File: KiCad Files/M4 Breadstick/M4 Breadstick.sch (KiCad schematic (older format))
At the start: 79 parts, among them IC1 ATSAMD51G_TQFN48, J10 D6|A6|RX, J11 D3|A3, J12 D4|A4, J13 D1|A1, J14 D14|SDA, J15 D20|A20, J16 D15|SCL, J17 D16, J18 D13|SCK, J19 D17, J2 3220-10-0300-00-TR, J20 D12|MISO, J21 VBUS, J22 D11|MOSI, J23 D10|COM3, J24 D9|COM2, J25 D8|SDA, J26 D7|SCL, J27 VBAT, J28 GND, J29 3.3V, J3 GND, J30 3.3V, J4 ~RESET, J5 D2|A2|LDAC, J6 AREF, J7 D19|A19, J8 D18|A18|RDAC, J9 D5|A5|TX, SW1 SMD-BUTTON_2P-3.0X2.5X1.2+0.4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, U1 SN74LVC2T45DCUR, U2 GD25x16, U3 NCP1117ST33T3G

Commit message: Multi sheets created
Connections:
- net VHI: no longer C1.1, C10.1, C9.1, D1.2 (-), D2.2 (-), U3.3 (IN)
- new net 5V: C1.1, C10.1, C9.1, D1.2 (-), D2.2 (-), U3.3 (IN)
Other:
- moved on the sheet: C1, C10, C2, C3, C4, C5, C6, C7, C8, C9, D1, D2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

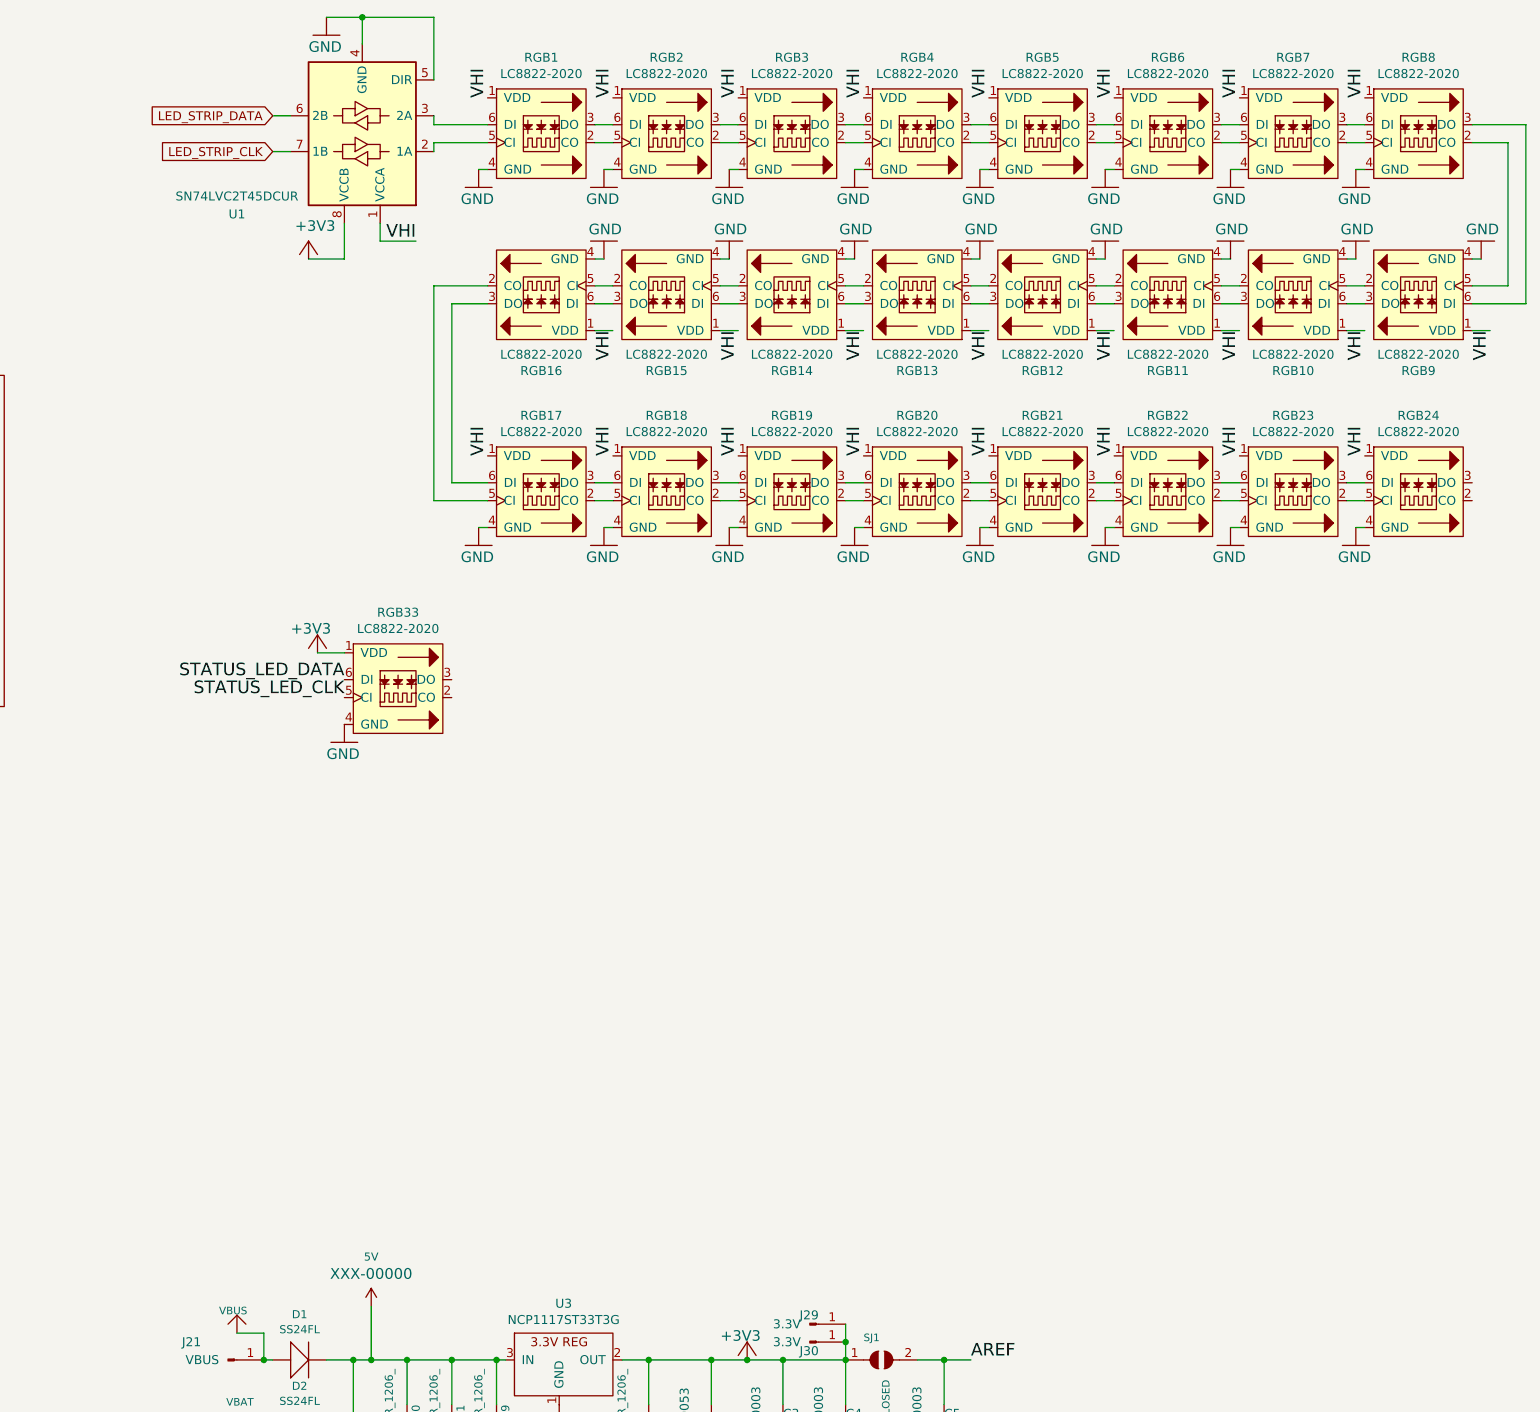
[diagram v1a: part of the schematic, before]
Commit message: LEDs moved to child sheet
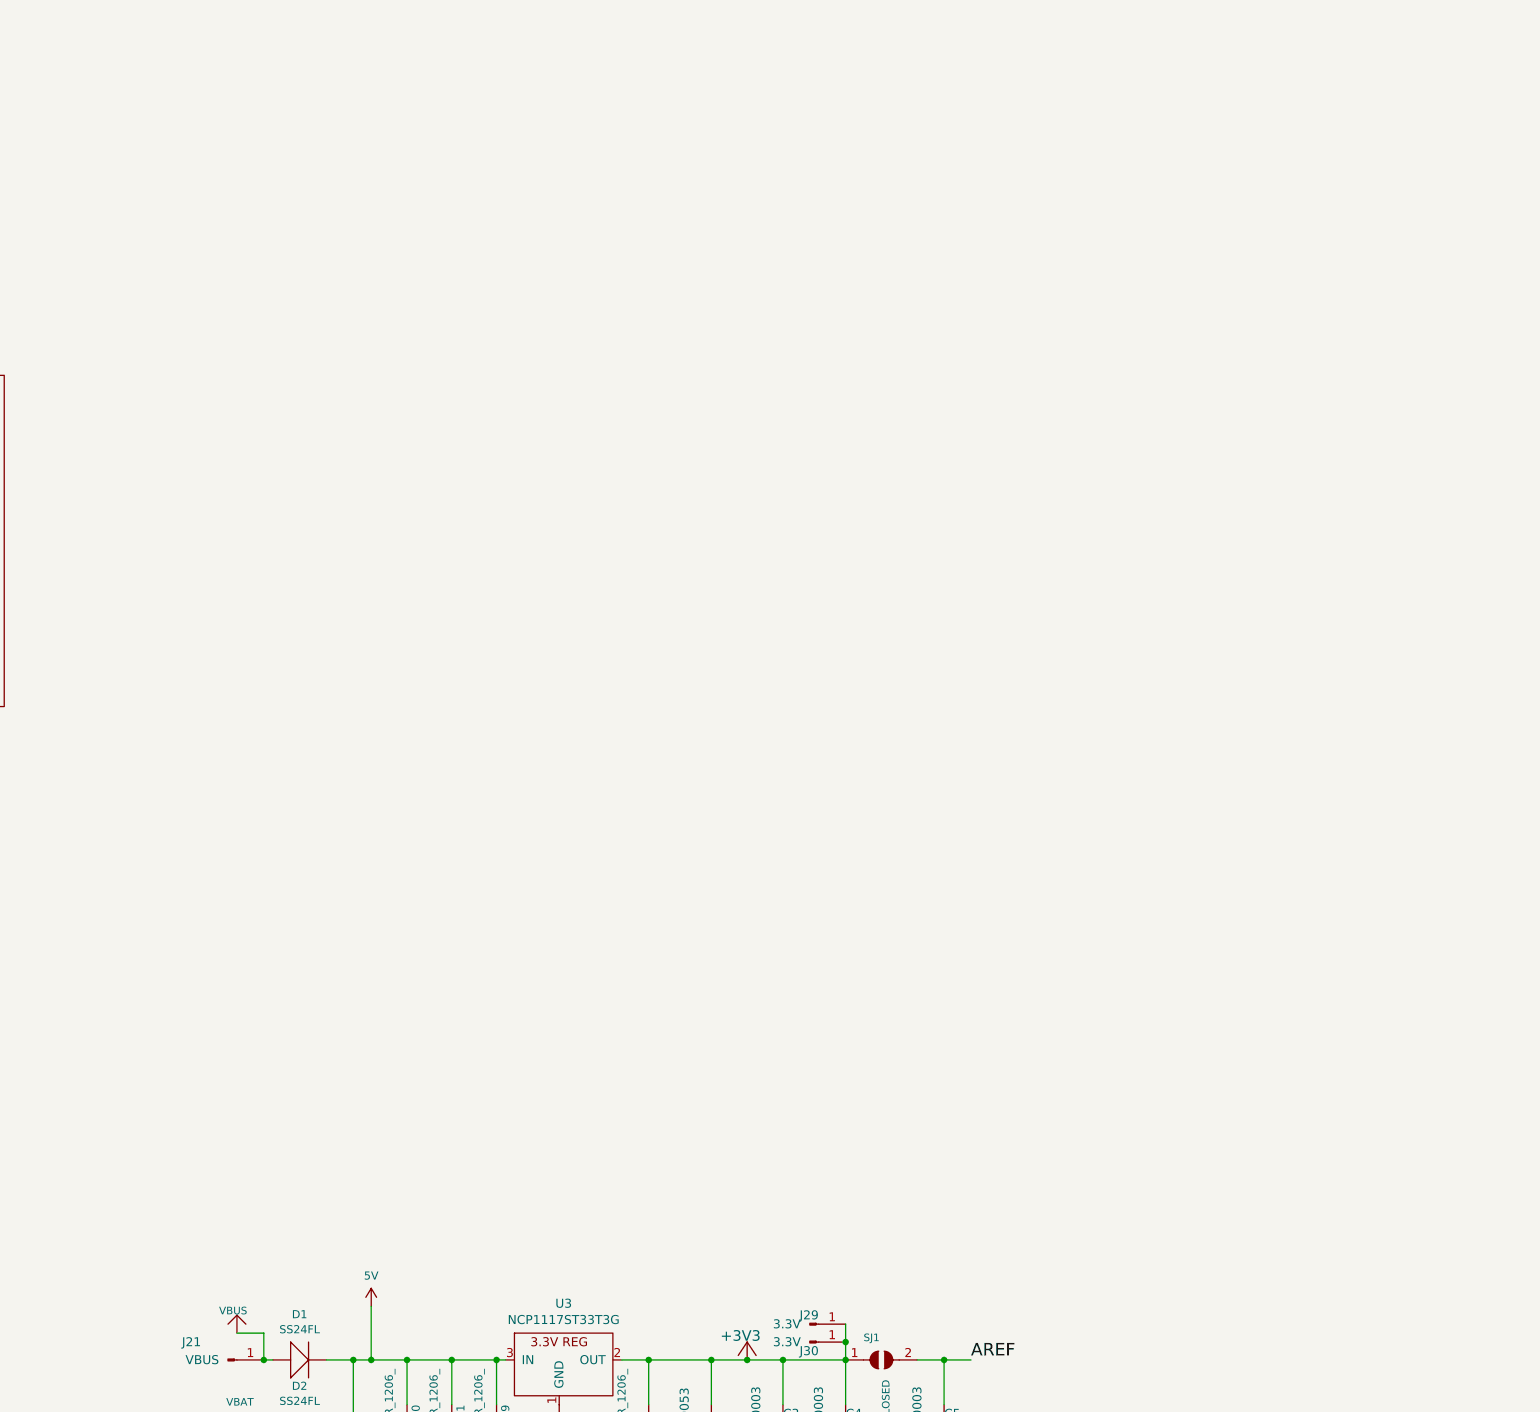
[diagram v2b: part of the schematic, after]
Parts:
- removed RGB1, RGB10, RGB11, RGB12, RGB13, RGB14, RGB15, RGB16, RGB17, RGB18, RGB19, RGB2, RGB20, RGB21, RGB22, RGB23, RGB24, RGB3, RGB33, RGB4, RGB5, RGB6, RGB7, RGB8, RGB9: LC8822-2020, MichaelRangen_Footprints:LC8822-2020, symbol M4-Breadstick-rescue:LC8822-2020-MichaelRangen_SchematicSymbols
- removed U1: SN74LVC2T45DCUR, Housings_SSOP:VSSOP-8_2.3x2mm_Pitch0.5mm, symbol Logic_LevelTranslator:74LVC2T45DC
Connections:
- net labels removed: VHI
- wire segments 199 -> 98

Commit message: page template done
needs review from mike
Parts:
- removed C1, C10, C8, C9: CERAMIC-100UF-6.3V-20%-X5R_1206_, OPL_Capacitor:C1206, symbol M4-Breadstick-rescue:CERAMIC-100UF-6.3V-20%-X5R_1206_-OPL_Capacitor
- removed C2: 10uF_6.3V_0402_302010053, OPL_Capacitor:C0402, symbol Device:C
- removed C3, C4: 1uF_6.3V_0402_302010003, OPL_Capacitor:C0402, symbol Device:C
- removed D1, D2: SS24FL, OPL_Discrete_Semiconductor:SOD-123, symbol M4-Breadstick-rescue:SMD-DIODE-SCHOTTKY-20V-1A_SOD-123_-OPL_Discrete_Semiconduc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
- removed J21: VBUS, Pin_Headers:Pin_Header_Straight_1x01_Pitch2.54mm, symbol Connector:Conn_01x01_Male
- removed J27: VBAT, Pin_Headers:Pin_Header_Straight_1x01_Pitch2.54mm, symbol Connector:Conn_01x01_Male
- removed J29, J30: 3.3V, Pin_Headers:Pin_Header_Straight_1x01_Pitch2.54mm, symbol Connector:Conn_01x01_Male
- removed U3: NCP1117ST33T3G, digikey-footprints:SOT-223, symbol M4-Breadstick-rescue:NCP1117ST33T3G-MichaelRangen_SchematicSymbols
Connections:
- net labels removed: 5V, VBAT
- wire segments 98 -> 73
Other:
- moved on the sheet: C6, C7, D3, IC1A, IC1B, J10, J11, J12, J13, J14, J15, J16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
